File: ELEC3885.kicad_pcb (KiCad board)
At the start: 4 copper layers, 190 x 130 mm, 127 parts, among them J1 MicInstIn, J2 LineIn, J3 HeadPhoneOut, J4 LineOutR, J5 LineOutL, J6 Conn_LiPo, J7 USB_B_Micro, J9 Conn_01x05_Female, SW1 SW_SPST, SW10 SW_Push, SW11 SW_Push, SW12 SW_Push, SW5 SW_Push, SW6 SW_Push, SW7 SW_Push, SW8 SW_Push, SW9 SW_Push, U1 AP7313, U10 MT3608, U11 L7805, U2 SGTL5000XNLA3, U3 Teensy4.1, U4 74HC595, U5 74HC595, U6 74HC595, U7 LCD_Conn, U8 NE5532, U9 MCP73831-2-OT

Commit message: Encoders, RGB LED added, PCB cleanup
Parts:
- added JP4: Jumper_3_Bridged12, Jumper:SolderJumper-3_P1.3mm_Bridged2Bar12_RoundedPad1.0x1.5mm_NumberLabels, F.Cu at (229.1, 30.6)
- added R51: 100, Resistor_SMD:R_0402_1005Metric, F.Cu at (76.1, 97.5)
- added R52: 100, Resistor_SMD:R_0402_1005Metric, F.Cu at (83.5, 101.8)
- added R53: 100, Resistor_SMD:R_0402_1005Metric, F.Cu at (103.5, 101.8)
- added R54: 100, Resistor_SMD:R_0402_1005Metric, F.Cu at (123.5, 101.8)
- added R55: 100, Resistor_SMD:R_0402_1005Metric, F.Cu at (141.6, 101.3)
- added R56: 100R, Resistor_SMD:R_0402_1005Metric, F.Cu at (-34.6, 120.2)
- added R57: 100R, Resistor_SMD:R_0402_1005Metric, F.Cu at (-34.6, 122.2)
- added R58: 100R, Resistor_SMD:R_0402_1005Metric, F.Cu at (-34.6, 124.2)
- added R59: 100R, Resistor_SMD:R_0402_1005Metric, F.Cu at (-34.6, 126.2)
- added R60: 100R, Resistor_SMD:R_0402_1005Metric, F.Cu at (-42.4, 114.6)
- added SW10: RotaryEncoder_Switch, Rotary_Encoder:RotaryEncoder_Alps_EC11E-Switch_Vertical_H20mm, F.Cu at (70.7, 114.6)
- added SW11: RotaryEncoder_Switch, Rotary_Encoder:RotaryEncoder_Alps_EC11E-Switch_Vertical_H20mm, F.Cu at (90.8, 114.5)
- added SW12: RotaryEncoder_Switch, Rotary_Encoder:RotaryEncoder_Alps_EC11E-Switch_Vertical_H20mm, F.Cu at (110.9, 114.6)
- added SW13: RotaryEncoder_Switch, Rotary_Encoder:RotaryEncoder_Alps_EC11E-Switch_Vertical_H20mm, F.Cu at (131.0, 114.6)
- added SW14: SW_Push, Button_Switch_SMD:SW_Push_1P1T_NO_6x6mm_H9.5mm, F.Cu at (-41.3, 79.1)
- added SW15: SW_Push, Button_Switch_SMD:SW_Push_1P1T_NO_6x6mm_H9.5mm, F.Cu at (-41.3, 86.7)
- added SW16: SW_Push, Button_Switch_SMD:SW_Push_1P1T_NO_6x6mm_H9.5mm, F.Cu at (-41.3, 94.3)
- added SW17: SW_Push, Button_Switch_SMD:SW_Push_1P1T_NO_6x6mm_H9.5mm, F.Cu at (-41.3, 101.9)
- added TP5: TP_BUTTON_ARRAY, TestPoint:TestPoint_Pad_D1.0mm, F.Cu at (-39.5, 107.2)
- TP1: renamed from TP5; value TP_BUTTON_ARRAY -> TP_SEQUENCE_ARRAY
- moved H1 249.9 mm to (58.1, 33.3)
- moved H4 249.7 mm to (58.1, 94.2)
- moved H3 167.4 mm to (149.5, 94.2)
- moved H2 167.1 mm to (149.5, 33.3)
- moved D11 110.5 mm to (191.8, 132.7), turned to -90 degrees
- moved D5 110.4 mm to (108.1, 132.7), turned to -90 degrees
- moved D7 106.6 mm to (175.1, 132.7)
- moved D4 106.4 mm to (76.6, 134.5), turned to 180 degrees
- moved D6 106.2 mm to (141.6, 132.7)
- moved R39 106.0 mm to (74.1, 129.7), turned to -90 degrees
- moved R31 105.5 mm to (124.0, 130.2), turned to -90 degrees
- moved D8 105.3 mm to (91.3, 132.7)
- moved R27 105.1 mm to (75.3, 129.7), turned to -90 degrees
- moved D9 104.9 mm to (160.2, 134.7), turned to 180 degrees
- moved R34 104.6 mm to (157.8, 129.9), turned to -90 degrees
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- renumbered C17 to C10, C16 to C11, C9 to C12, C10 to C13, C11 to C14, C12 to C15, C18 to C16, C13 to C17, C14 to C18, C15 to C2, C2 to C3, C3 to C4, C4 to C5, C5 to C6, C6 to C7, C7 to C8, C8 to C9, D9 to D1, D4 to D10, D8 to D11, D10 to D2, D11 to D3, D1 to D4, D3 to D5, D5 to D6, D2 to D8, D6 to D9, J9 to J4, J4 to J5, J5 to J6, J6 to J8, JP2 to JP1, JP1 to JP2, R40 to R1, R44 to R10, R45 to R11, R46 to R12, R47 to R13, R4 to R14, R48 to R15, R49 to R16, R50 to R17, R5 to R18, R6 to R19, R41 to R2, R7 to R20, R8 to R21, R9 to R22, R10 to R23, R11 to R24, R12 to R25, R13 to R26, R30 to R27, R31 to R28, R32 to R29, R1 to R3, R33 to R30, R22 to R31, R23 to R32, R24 to R33, R25 to R34, R20 to R35, R18 to R36, R16 to R37, R14 to R38, R34 to R39, R2 to R4, R35 to R40, R36 to R41, R37 to R42, R26 to R43, R27 to R44, R28 to R45, R29 to R46, R21 to R47, R19 to R48, R17 to R49, R3 to R5, R15 to R50, R38 to R6, R39 to R7, R42 to R8, R43 to R9, SW5 to SW2, SW6 to SW3, SW7 to SW4, SW8 to SW5, SW9 to SW6, SW10 to SW7, SW11 to SW8, SW12 to SW9, TP4 to TP2, TP1 to TP4, U8 to U1, U5 to U10, U7 to U11, U1 to U2, U2 to U3, U3 to U4, U9 to U5, U10 to U6, U11 to U7, U6 to U8, U4 to U9
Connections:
- C17 pad 1: Net-(D9-K) -> Net-(JP4-A)
- D1 pad 1: Net-(D9-K) -> Net-(D1-K)
- J7 pad 1: Net-(D9-K) -> Net-(D1-K)
- R15 pad 1: Net-(D9-K) -> Net-(JP4-A)
- R26 pad 2: /Teensy/BUTTON_ARRAY -> /Teensy/SEQUENCE_ARRAY
- SW2 pad 2: /Teensy/BUTTON_ARRAY -> /Teensy/SEQUENCE_ARRAY
- SW3 pad 2: /Teensy/BUTTON_ARRAY -> /Teensy/SEQUENCE_ARRAY
- SW4 pad 2: /Teensy/BUTTON_ARRAY -> /Teensy/SEQUENCE_ARRAY
- SW5 pad 2: /Teensy/BUTTON_ARRAY -> /Teensy/SEQUENCE_ARRAY
- SW6 pad 2: /Teensy/BUTTON_ARRAY -> /Teensy/SEQUENCE_ARRAY
- SW7 pad 2: /Teensy/BUTTON_ARRAY -> /Teensy/SEQUENCE_ARRAY
- SW8 pad 2: /Teensy/BUTTON_ARRAY -> /Teensy/SEQUENCE_ARRAY
- SW9 pad 2: /Teensy/BUTTON_ARRAY -> /Teensy/SEQUENCE_ARRAY
- TP1 pad 1: /Teensy/BUTTON_ARRAY -> /Teensy/SEQUENCE_ARRAY
- U4 pad 23: unconnected-(U3-31_CTX3-Pad23) -> /Teensy/ENCODER_1_B
- U4 pad 24: unconnected-(U3-32_OUT1B-Pad24) -> /Teensy/ENCODER_1_A
- U4 pad 25: unconnected-(U3-33_MCLK2-Pad25) -> /Teensy/ENCODER_4_B
- U4 pad 26: unconnected-(U3-34_RX8-Pad26) -> /Teensy/ENCODER_4_A
- U4 pad 27: unconnected-(U3-35_TX8-Pad27) -> /Teensy/ENCODER_3_B
- U4 pad 28: unconnected-(U3-36_CS-Pad28) -> /Teensy/ENCODER_3_A
- U4 pad 29: unconnected-(U3-37_CS-Pad29) -> /Teensy/ENCODER_2_B
- U4 pad 30: unconnected-(U3-38_CS1_IN1-Pad30) -> /Teensy/ENCODER_2_A
- U4 pad 31: unconnected-(U3-39_MISO1_OUT1A-Pad31) -> /Teensy/ENCODER_SW_ARRAY
- U4 pad 32: unconnected-(U3-40_A16-Pad32) -> /Teensy/SEQUENCE_ARRAY
- U5 pad 4: Net-(D9-K) -> Net-(JP4-A)
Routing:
- net /Teensy/ENCODER_1_A: track 0.00 -> 196.3 mm
- net /Teensy/ENCODER_1_B: track 0.00 -> 182.1 mm, vias 0 -> 1
- net /Teensy/ENCODER_SW_ARRAY: track 0.00 -> 164.5 mm, vias 0 -> 2
- net /Teensy/ENCODER_2_A: track 0.00 -> 152.2 mm
- net /Teensy/ENCODER_2_B: track 0.00 -> 142.3 mm
- net /Teensy/ENCODER_3_A: track 0.00 -> 129.9 mm
- net /Teensy/ENCODER_3_B: track 0.00 -> 127.3 mm
- net /Teensy/ENCODER_4_A: track 0.00 -> 115.2 mm
- net /Teensy/ENCODER_4_B: track 0.00 -> 111.9 mm
- net +3.3V: track 192.8 -> 288.4 mm
- net +5V: track 235.1 -> 290.7 mm, vias 5 -> 12
- net /Teensy/LCD_DC: track 208.8 -> 159.9 mm
- net Net-(U10-QH'): track 0.00 -> 47.6 mm, vias 0 -> 2
- net /Teensy/LCD_CS: track 206.8 -> 163.5 mm
- net /Teensy/LED_RCLK: track 112.8 -> 153.5 mm, vias 8 -> 4
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
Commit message: Rev3 layout work
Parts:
- SW14, SW15, SW16, SW17, SW2, SW3, SW4, SW5, SW6, SW7, SW8, SW9: footprint Button_Switch_SMD:SW_Push_1P1T_NO_6x6mm_H9.5mm -> Button_Switch_Keyboard:SW_Cherry_MX_1.00u_PCB
- moved TP5 245.0 mm to (205.5, 104.8)
- moved R60 244.8 mm to (202.3, 109.3), turned to -90 degrees
- moved SW17 242.5 mm to (201.0, 113.7)
- moved R59 236.3 mm to (201.0, 109.3), turned to 90 degrees
- moved R58 223.7 mm to (188.8, 113.5)
- moved SW16 223.4 mm to (181.3, 113.7)
- moved SW15 204.5 mm to (161.5, 113.7)
- moved R57 203.6 mm to (168.8, 113.5)
- moved SW14 186.2 mm to (141.7, 113.7)
- moved R56 183.8 mm to (149.0, 113.8)
- moved TP2 150.6 mm to (123.6, 130.2)
- moved R26 57.2 mm to (191.6, 145.4), turned to -90 degrees
- moved TP1 57.1 mm to (190.6, 138.1)
- moved SW9 56.8 mm to (186.1, 146.8), turned to 0 degrees
- moved R25 54.8 mm to (185.4, 143.5), turned to 180 degrees
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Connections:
- R26 pad 1: Net-(R24-Pad2) -> GND
- R60 pad 1: Net-(R58-Pad2) -> GND
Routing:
- net /Teensy/SEQUENCE_ARRAY: track 0.00 -> 210.1 mm, vias 0 -> 2
- net +5V: track 290.7 -> 428.8 mm, vias 12 -> 19
- net /Teensy/BUTTON_ARRAY: track 0.00 -> 112.8 mm, vias 0 -> 2
- net +3.3V: track 288.4 -> 365.2 mm, vias 7 -> 8
- net /Audio/HP_R: track 113.4 -> 139.6 mm
- net /Audio/HP_L: track 129.0 -> 152.6 mm
- net Net-(R57-Pad2): track 0.00 -> 19.1 mm
- net Net-(R56-Pad2): track 0.00 -> 18.8 mm
- net /Audio/HP_VGND: track 118.1 -> 134.8 mm
- net /Audio/MEMS_IN: track 92.3 -> 108.9 mm
- net Net-(R58-Pad2): track 0.00 -> 15.6 mm
- net Net-(U8-SER): track 61.2 -> 71.9 mm, vias 0 -> 4
- net Net-(U10-~{OE}): track 95.6 -> 105.0 mm, vias 2 -> 0
- net Net-(R24-Pad2): track 6.10 -> 14.9 mm
- net Net-(D10-RA): track 4.01 -> 12.3 mm
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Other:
- board size 190 x 130 mm -> 190 x 145.2 mm
- board text removed: "HEADPHONE"
- board text removed: "INTERNAL MIC"
- board text removed: "LCD"
- board text removed: "LINE IN"
- board text removed: "LINE OUT"
- board text removed: "MIC IN"
- board text removed: "SD CARD SLOT"
- board text removed: "USB PWR"

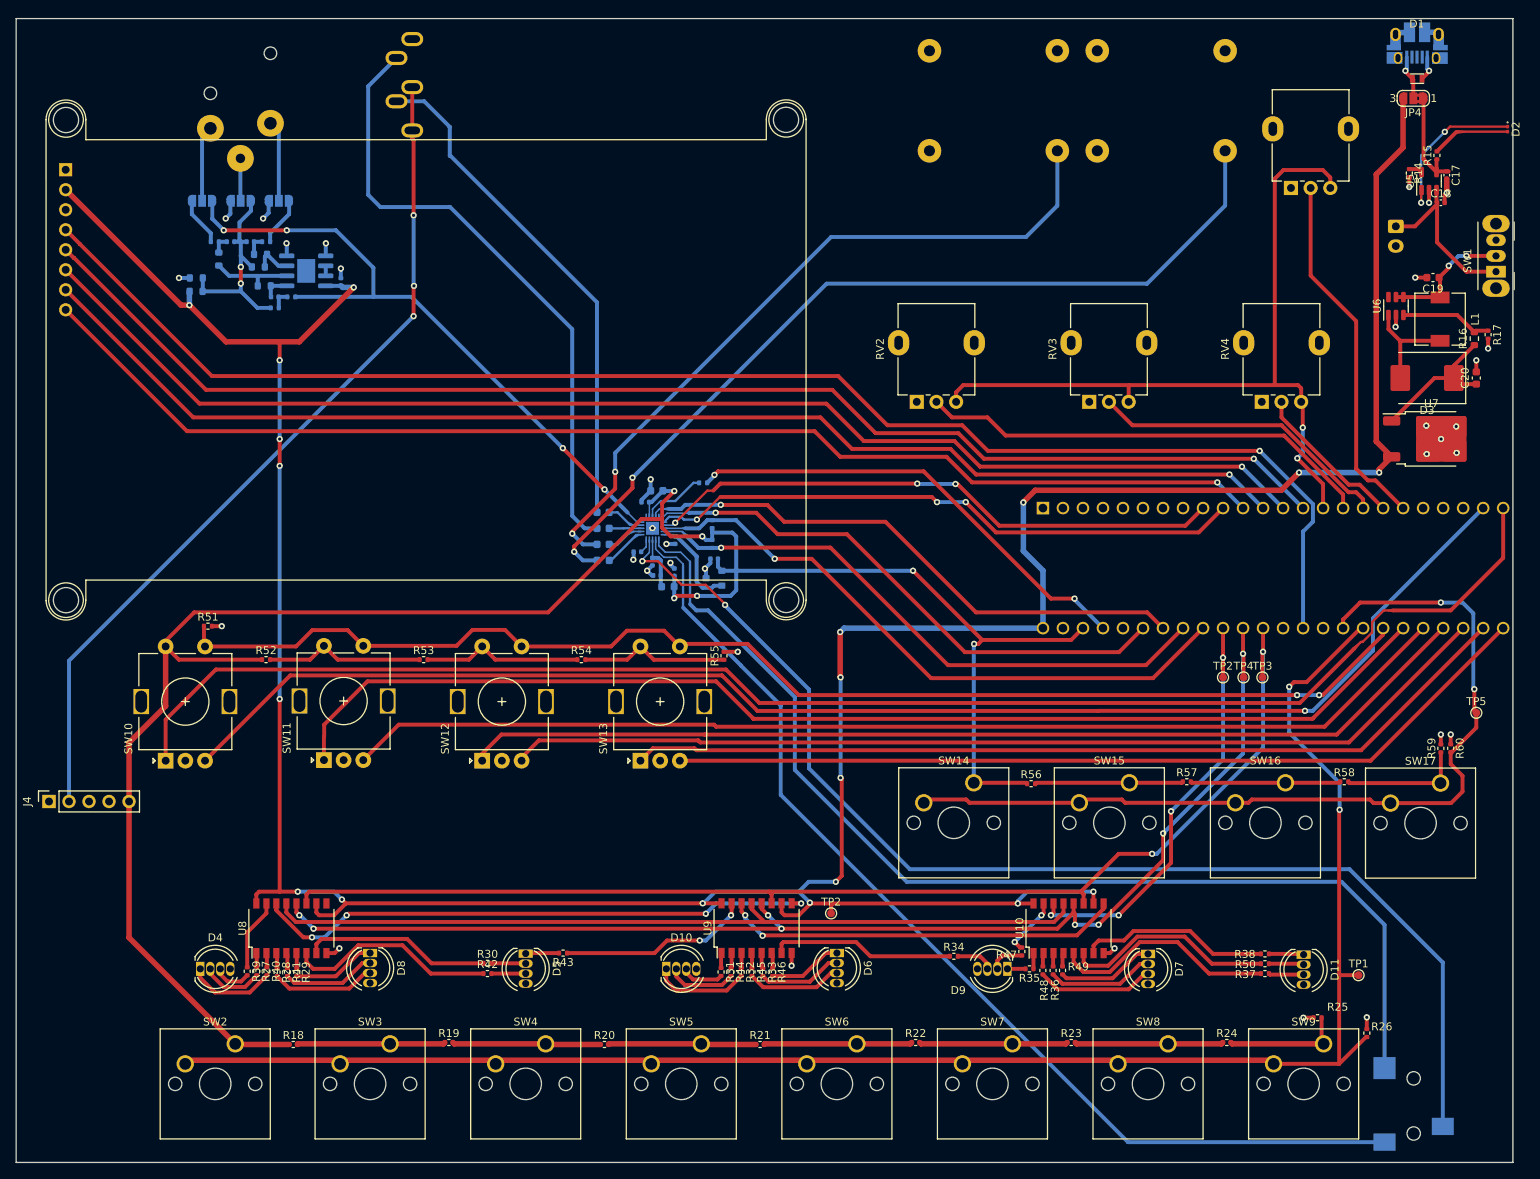
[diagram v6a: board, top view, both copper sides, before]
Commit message: Testpoints added, silkscreen cleaned
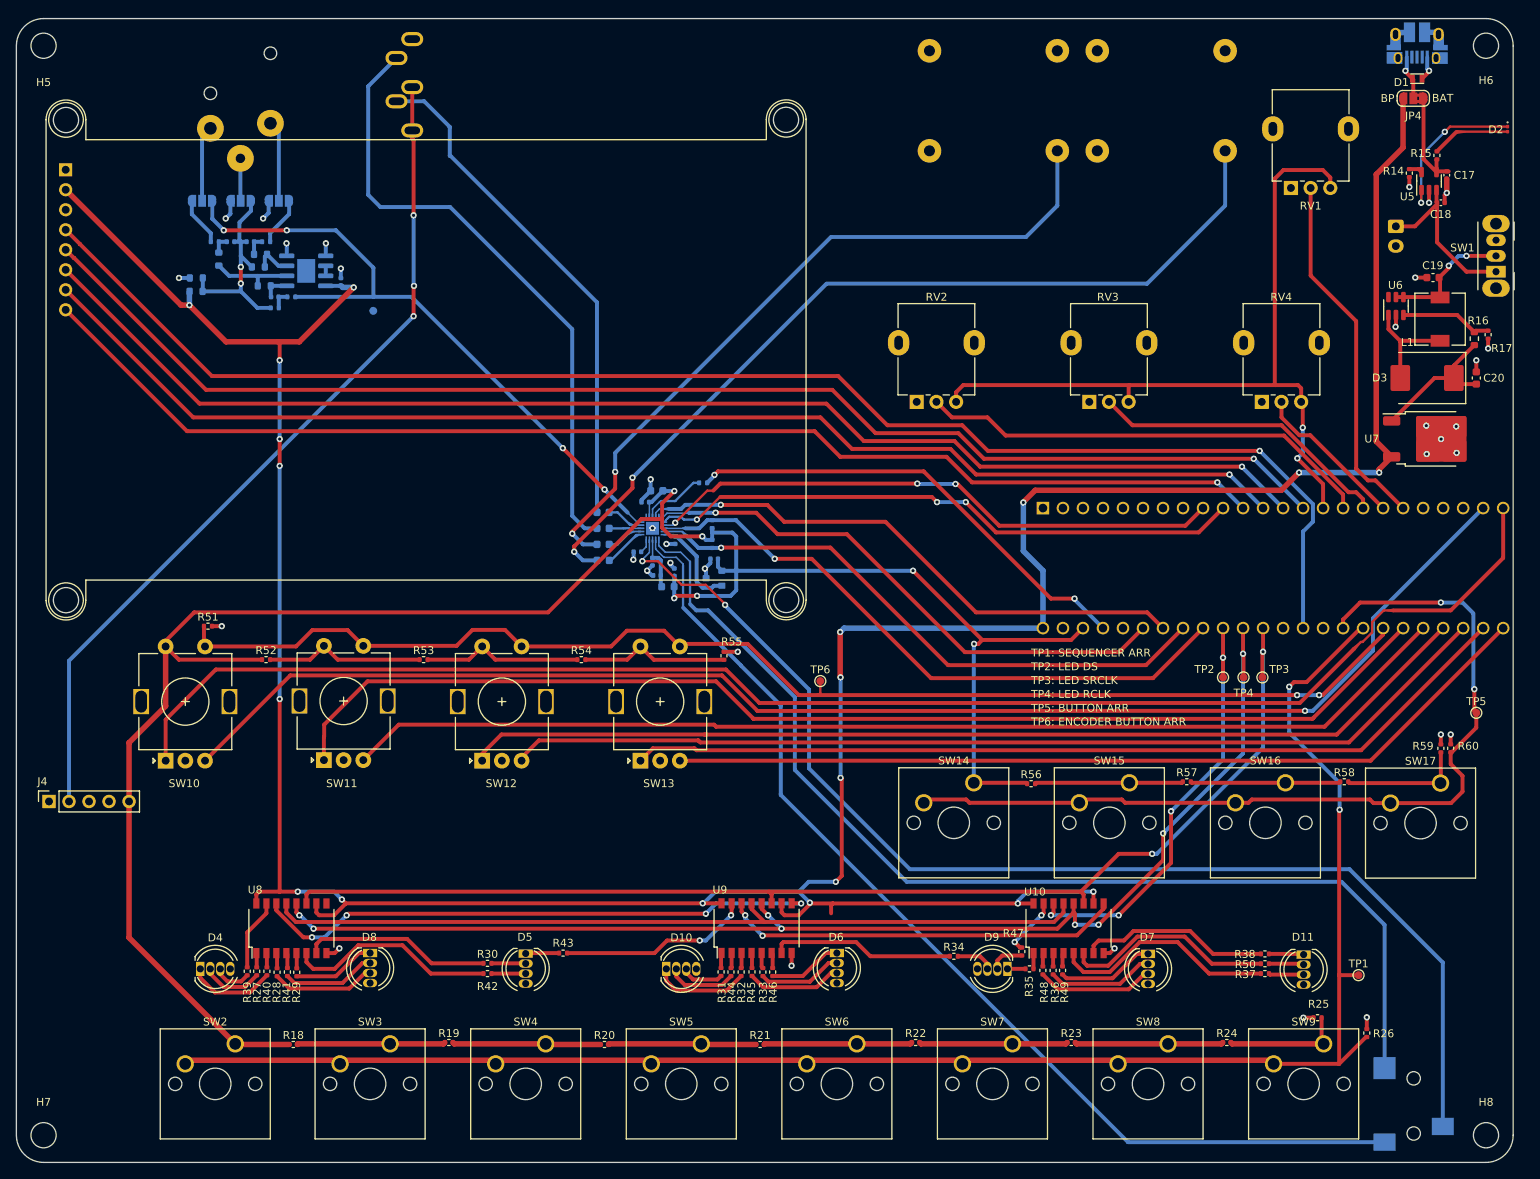
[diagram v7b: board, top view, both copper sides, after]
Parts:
- removed the TP2 at (123.6, 130.2)
- added H5: MountingHole, MountingHole:MountingHole_3.2mm_M3, F.Cu at (23.6, 20.1)
- added H6: MountingHole, MountingHole:MountingHole_3.2mm_M3, F.Cu at (206.8, 20.1)
- added H7: MountingHole, MountingHole:MountingHole_3.2mm_M3, F.Cu at (23.6, 158.4)
- added H8: MountingHole, MountingHole:MountingHole_3.2mm_M3, F.Cu at (206.8, 158.4)
- added TP6: TP_ENCODER_ARRAY, TestPoint:TestPoint_Pad_D1.0mm, F.Cu at (122.2, 100.8)
- added TP7: TP_DIFF_OUT, TestPoint:TestPoint_Pad_D1.0mm, B.Cu at (65.5, 53.8)
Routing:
- net /Teensy/ENCODER_SW_ARRAY: track 164.0 -> 165.9 mm
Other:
- outline, holes or cut-outs redrawn
- board text added: "TP1: SEQUENCER ARR"
- board text added: "TP2: LED DS"
- board text added: "TP3: LED SRCLK"
- board text added: "TP4: LED RCLK"
- board text added: "TP5: BUTTON ARR"
- board text added: "TP6: ENCODER BUTTON ARR"
- board text added: "TP7: DIFF AMP OUT"
